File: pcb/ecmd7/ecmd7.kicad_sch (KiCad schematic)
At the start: 75 parts, among them J1 Conn_02x06_Odd_Even, J2 Conn_02x06_Odd_Even, J3 Conn_02x06_Odd_Even, J4 Conn_01x02_Socket, J5 DE9_Socket, J6 Conn_01x04_Socket, Q1 IRFS3806, Q2 IRFS3806, Q3 IRFS3806, Q4 IRFS3806, Q5 IRFS3806, Q6 IRFS3806, Q7 BSC098N10NS5, Q8 BSC098N10NS5, U1 TMC6200-TA, U3 LM5118MH

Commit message: Finalize schematic Add ESD protection Align connector pinout with Arty A7 and Zybo Z7 PMOD
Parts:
- removed J5: DE9_Socket, symbol Connector:DE9_Socket
- removed J6: Conn_01x04_Socket, Connector_PinHeader_1.27mm:PinHeader_1x04_P1.27mm_Vertical, symbol Connector:Conn_01x04_Socket
- removed R44, R45: 4.7k, Resistor_SMD:R_0805_2012Metric, symbol Device:R
- added C11, C38, C42, C43, C57: 100n, Capacitor_SMD:C_0805_2012Metric, symbol Device:C
- added C12, C37, C48: 1u, Capacitor_SMD:C_0805_2012Metric, symbol Device:C
- added D3, D4: SK220ATR, Diode_SMD:D_SMA, symbol Device:D_Schottky
- added D5, D7: MBR0530, Diode_SMD:D_SOD-123, symbol Diode:MBR0530
- added D6, D8: D, Diode_SMD:D_MiniMELF, symbol Device:D
- added J5: Encoder, Connector_PinHeader_2.54mm:PinHeader_2x04_P2.54mm_Vertical, symbol Connector_Generic:Conn_02x04_Odd_Even
- added J7: RS422/BISS-C, Connector_PinHeader_2.54mm:PinHeader_2x03_P2.54mm_Vertical, symbol Connector_Generic:Conn_02x03_Odd_Even
- added JP1, JP3, JP4, JP5, JP7: SolderJumper_2_Open, Jumper:SolderJumper-2_P1.3mm_Open_RoundedPad1.0x1.5mm, symbol Jumper:SolderJumper_2_Open
- added JP2, JP6: SolderJumper_2_Bridged, Jumper:SolderJumper-2_P1.3mm_Bridged_RoundedPad1.0x1.5mm, symbol Jumper:SolderJumper_2_Bridged
- added JP8: SolderJumper_2_Bridged, Jumper:SolderJumper-2_P1.3mm_Open_RoundedPad1.0x1.5mm, symbol Jumper:SolderJumper_2_Bridged
- added L3, L5: 10u, Inductor_SMD:L_TechFuse_SL0530, symbol Device:L
- added L4: 1u, Inductor_SMD:L_0805_2012Metric, symbol Device:L
- added R46, R50: 470, Resistor_SMD:R_0805_2012Metric, symbol Device:R
- added R47: 32k, Resistor_SMD:R_0805_2012Metric, symbol Device:R
- added R48, R51, R64: 10k, Resistor_SMD:R_0805_2012Metric, symbol Device:R
- added R49, R53: 10, Resistor_SMD:R_0805_2012Metric, symbol Device:R
- added R52: 16k, Resistor_SMD:R_0805_2012Metric, symbol Device:R
- added U6: TLV71318PDBV, Package_TO_SOT_SMD:SOT-23-5, symbol Regulator_Linear:TLV71318PDBV
- added U8, U9: LT1616ES6#TRPBF, Package_TO_SOT_SMD:SOT-23-6, symbol ssta_symbols:LT1616ES6#TRPBF
- C29, C30, C31, C32, C33, C34, C35, C36, C40, C55: footprint (none) -> Capacitor_SMD:C_0805_2012Metric
- D1, D2: value D_Schottky -> SK220ATR; footprint (none) -> Diode_SMD:D_SMA
- J1: renamed from J2; value Conn_02x06_Odd_Even -> PMOD_SPI_ENC; footprint Connector_PinHeader_1.27mm:PinHeader_2x06_P1.27mm_Horizontal -> Connector_PinHeader_2.54mm:PinHeader_2x06_P2.54mm_Horizontal
- J2: renamed from J3; value Conn_02x06_Odd_Even -> PMOD_ADC_MPIO; footprint Connector_PinHeader_1.27mm:PinHeader_2x06_P1.27mm_Horizontal -> Connector_PinHeader_2.54mm:PinHeader_2x06_P2.54mm_Horizontal
- J3: renamed from J1; value Conn_02x06_Odd_Even -> PMOD_DRV; footprint Connector_PinHeader_1.27mm:PinHeader_2x06_P1.27mm_Horizontal -> Connector_PinHeader_2.54mm:PinHeader_2x06_P2.54mm_Horizontal
- J4: footprint Connector_AMASS:AMASS_XT60-F_1x02_P7.20mm_Vertical -> Connector_AMASS:AMASS_XT60-M_1x02_P7.20mm_Vertical; symbol Connector:Conn_01x02_Socket -> Connector:Conn_01x02_Pin
- JU1: value Screw_Terminal_01x01 -> Phase U
- JV1: value Screw_Terminal_01x01 -> Phase V
- JW1: value Screw_Terminal_01x01 -> Phase W
- R15: footprint (none) -> Resistor_SMD:R_0805_2012Metric
- U1: footprint eTQFP48_9x9_TRI -> sst_footprints:eTQFP48_9x9_TRI
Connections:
- net +12V: now also D4.1 (K), JP1.2 (B), JP5.2 (B), JP8.2 (B), R46.1, U8.5 (VIN), U9.5 (VIN)
- net +3.3V: now also C48.1, D8.2 (A), JP4.2 (B), JP7.2 (B), L5.2, R52.2; no longer J1.1 (Pin_1), J1.2 (Pin_2), J2.1 (Pin_1), J2.2 (Pin_2), J3.1 (Pin_1), J3.2 (Pin_2)
- net +5V: now also C12.1, D6.2 (A), JP2.2 (B), JP6.2 (B), L3.2, L4.1, R47.2
- net GND: now also C12.2, C37.2, C38.2, C42.2, C48.2, C57.2, D5.2 (A), D7.2 (A), J5.7 (Pin_7), J7.5 (Pin_5), R48.2, R51.2, R64.1, U6.2 (GND), U8.2 (GND), U9.2 (GND)
- net at D1.2 (A), R15.1, U3.12 (CS): now also D3.2 (A)
- net at C33.2, D1.1 (K), L1.1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: now also D3.1 (K)
- net at D2.2 (A), L1.2, Q8.5 (D): now also D4.2 (A)
- net I2C_SCL renamed RS422_TX
- net I2C_SDA renamed RS422_RX
- new net: R47.1, R48.1, U8.3 (FB)
- new net: C43.2, D7.1 (K), L5.1, U9.6 (SW)
- new net: C43.1, D8.1 (K), U9.1 (BOOST)
- new net: C57.1, J7.6 (Pin_6), R53.2
- new net: JP5.1 (A), JP6.1 (A), JP7.1 (A), R53.1
- new net: JP8.1 (A), R50.1
- new net: JP3.2 (B), R50.2, R64.2, U9.4 (~{SHDN})
- new net: C11.1, D6.1 (K), U8.1 (BOOST)
- new net: C11.2, D5.1 (K), L3.1, U8.6 (SW)
- new net: C42.1, J5.8 (Pin_8), R49.2
- new net: R46.2, U8.4 (~{SHDN})
- new net: R51.1, R52.1, U9.3 (FB)
- new net: JP1.1 (A), JP2.1 (A), JP4.1 (A), R49.1
- new net +1V8A: U6.5 (OUT)
- new net +3.3V_IO: J1.1 (Pin_1), J1.2 (Pin_2), J2.1 (Pin_1), J2.2 (Pin_2), J3.1 (Pin_1), J3.2 (Pin_2), JP3.1 (A)
- new net +5VA: C37.1, C38.1, L4.2, U6.1 (IN), U6.3 (EN)
- new net ENC_A_N: J5.1 (Pin_1)
- new net ENC_A_P: J5.2 (Pin_2)
- new net ENC_B_N: J5.3 (Pin_3)
- new net ENC_B_P: J5.4 (Pin_4)
- new net ENC_Z_N: J5.5 (Pin_5)
- new net ENC_Z_P: J5.6 (Pin_6)
- new net RS422_RX_A: J7.4 (Pin_4)
- new net RS422_RX_B: J7.3 (Pin_3)
- new net RS422_TX_A: J7.2 (Pin_2)
- new net RS422_TX_B: J7.1 (Pin_1)
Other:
- sheet Feedback renamed ADC+IO
- sheet ADC+IO: file Feedback.kicad_sch -> ecmd7_adc_io.kicad_sch
- moved on the sheet: C19, C29, C30, C31, C32, C33, C34, C35, C36, C39, C40, C54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

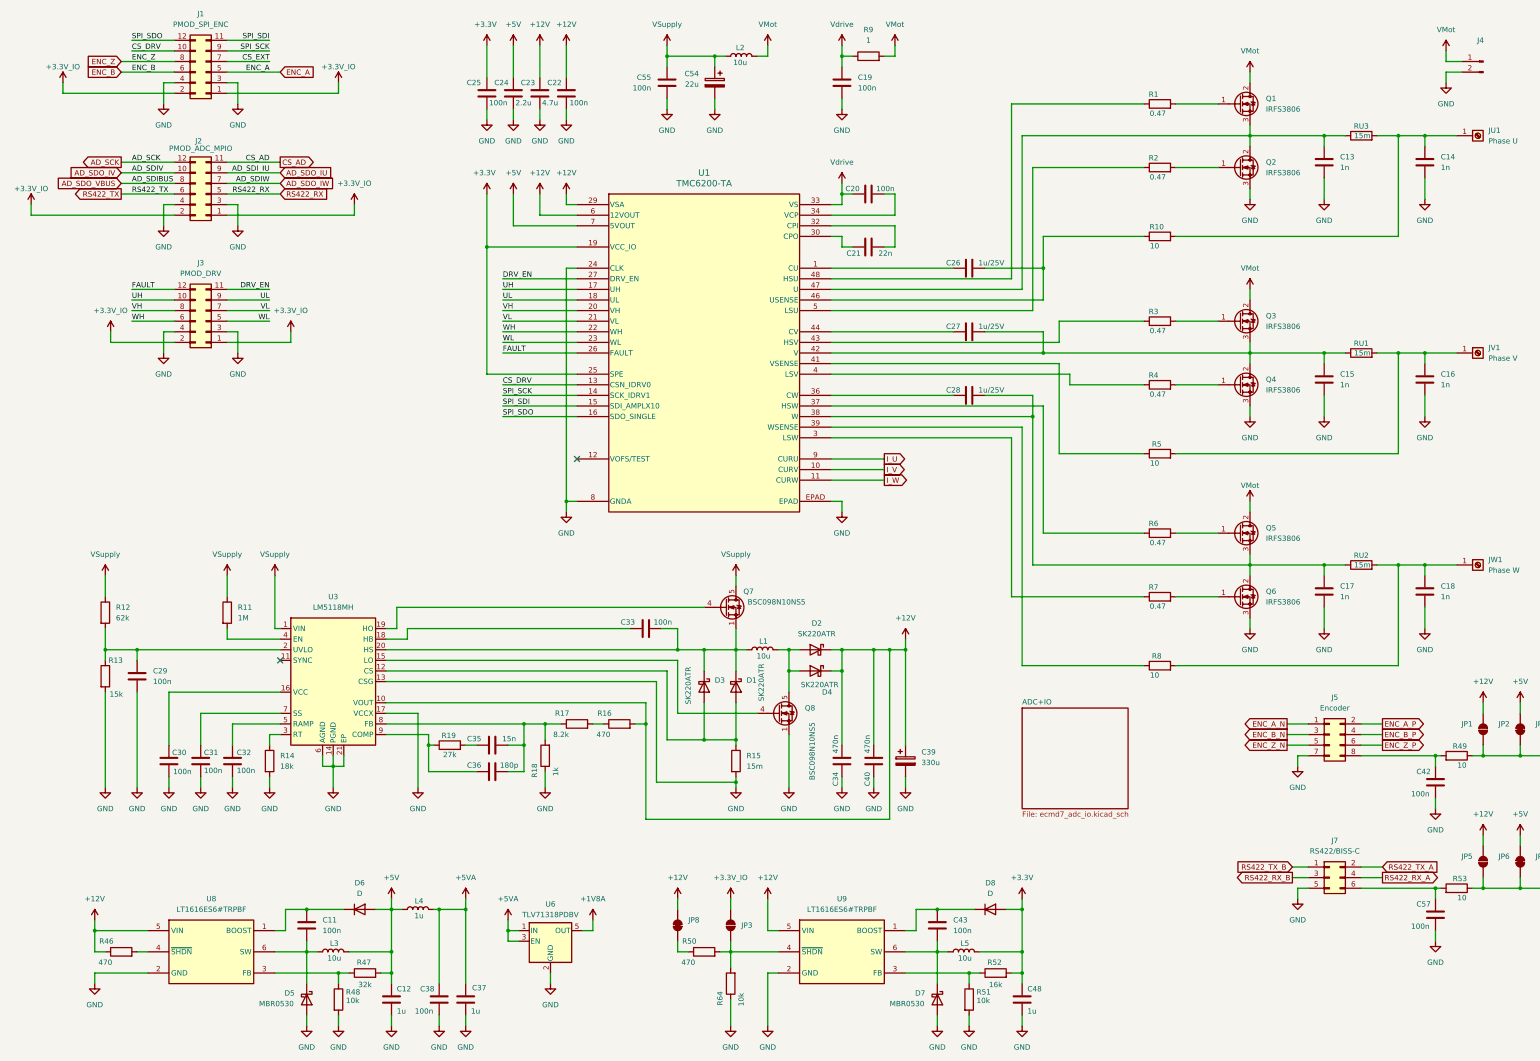
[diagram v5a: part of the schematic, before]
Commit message: Initial component placement
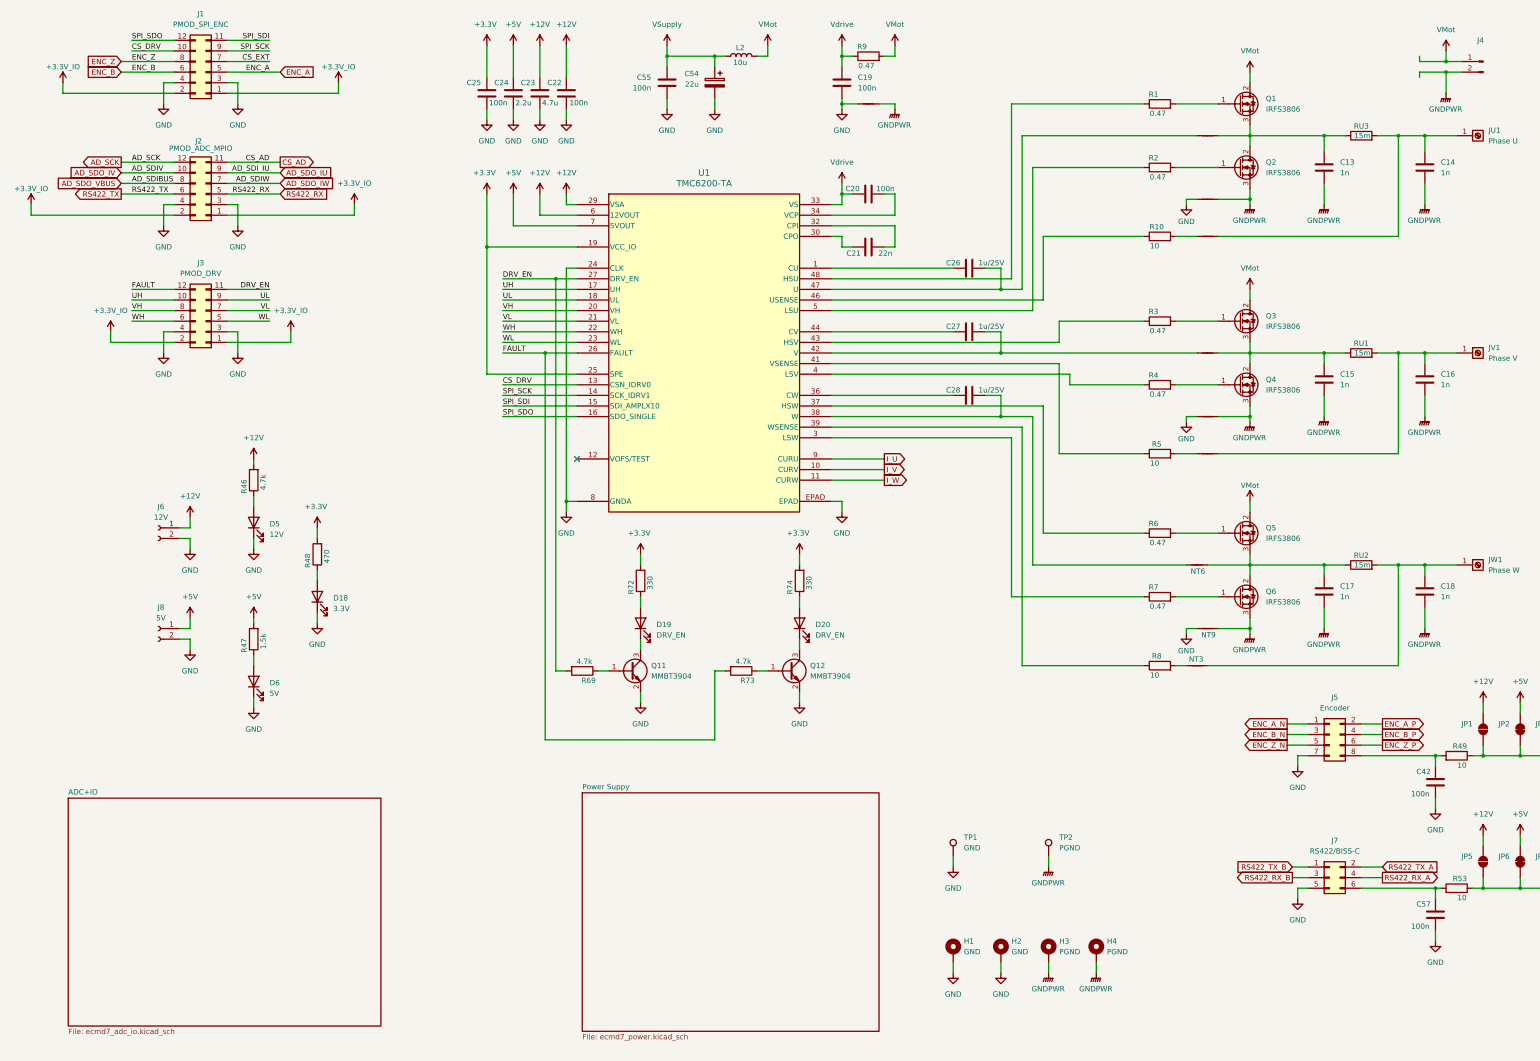
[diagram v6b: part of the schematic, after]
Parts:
- removed C11, C29, C30, C31, C32, C33, C38, C43: 100n, Capacitor_SMD:C_0805_2012Metric, symbol Device:C
- removed C12, C37, C48: 1u, Capacitor_SMD:C_0805_2012Metric, symbol Device:C
- removed C34, C40: 470n, Capacitor_SMD:C_0805_2012Metric, symbol Device:C
- removed C35: 15n, Capacitor_SMD:C_0805_2012Metric, symbol Device:C
- removed C36: 180p, Capacitor_SMD:C_0805_2012Metric, symbol Device:C
- removed C39: 330u, Capacitor_SMD:CP_Elec_6.3x9.9, symbol Device:C_Polarized
- removed D1, D2, D3, D4: SK220ATR, Diode_SMD:D_SMA, symbol Device:D_Schottky
- removed D5, D7: MBR0530, Diode_SMD:D_SOD-123, symbol Diode:MBR0530
- removed D6, D8: D, Diode_SMD:D_MiniMELF, symbol Device:D
- removed JP3: SolderJumper_2_Open, Jumper:SolderJumper-2_P1.3mm_Open_RoundedPad1.0x1.5mm, symbol Jumper:SolderJumper_2_Open
- removed JP8: SolderJumper_2_Bridged, Jumper:SolderJumper-2_P1.3mm_Open_RoundedPad1.0x1.5mm, symbol Jumper:SolderJumper_2_Bridged
- removed L1, L3, L5: 10u, Inductor_SMD:L_TechFuse_SL0530, symbol Device:L
- removed L4: 1u, Inductor_SMD:L_0805_2012Metric, symbol Device:L
- removed Q7, Q8: BSC098N10NS5, Package_TO_SOT_SMD:TDSON-8-1, symbol Transistor_FET:BSC098N10NS5
- removed R11: 1M, Resistor_SMD:R_0805_2012Metric, symbol Device:R
- removed R12: 62k, Resistor_SMD:R_0805_2012Metric, symbol Device:R
- removed R13: 15k, Resistor_SMD:R_0805_2012Metric, symbol Device:R
- removed R14: 18k, Resistor_SMD:R_0805_2012Metric, symbol Device:R
- removed R15: 15m, Resistor_SMD:R_0805_2012Metric, symbol Device:R
- removed R16, R50: 470, Resistor_SMD:R_0805_2012Metric, symbol Device:R
- removed R17: 8.2k, Resistor_SMD:R_0805_2012Metric, symbol Device:R
- removed R18: 1k, Resistor_SMD:R_0805_2012Metric, symbol Device:R
- removed R19: 27k, Resistor_SMD:R_0805_2012Metric, symbol Device:R
- removed R51, R64: 10k, Resistor_SMD:R_0805_2012Metric, symbol Device:R
- removed R52: 16k, Resistor_SMD:R_0805_2012Metric, symbol Device:R
- removed U3: LM5118MH, Package_SO:Texas_PWP0020A, symbol Regulator_Switching:LM5118MH
- removed U6: TLV71318PDBV, Package_TO_SOT_SMD:SOT-23-5, symbol Regulator_Linear:TLV71318PDBV
- removed U8, U9: LT1616ES6#TRPBF, Package_TO_SOT_SMD:SOT-23-6, symbol ssta_symbols:LT1616ES6#TRPBF
- added D18: 3.3V, Diode_SMD:D_0805_2012Metric, symbol Device:LED
- added D19, D20: DRV_EN, Diode_SMD:D_0805_2012Metric, symbol Device:LED
- added D5: 12V, Diode_SMD:D_0805_2012Metric, symbol Device:LED
- added D6: 5V, Diode_SMD:D_0805_2012Metric, symbol Device:LED
- added H1, H2: GND, MountingHole:MountingHole_3.2mm_M3_Pad_Via, symbol Mechanical:MountingHole_Pad
- added H3, H4: PGND, MountingHole:MountingHole_3.2mm_M3_Pad_Via, symbol Mechanical:MountingHole_Pad
- added J6: 12V, Connector_PinHeader_2.00mm:PinHeader_1x02_P2.00mm_Vertical, symbol Connector:Conn_01x02_Socket
- added J8: 5V, Connector_PinHeader_2.00mm:PinHeader_1x02_P2.00mm_Vertical, symbol Connector:Conn_01x02_Socket
- added NT1, NT2, NT3, NT4, NT5, NT6: NetTie_2, NetTie:NetTie-2_SMD_Pad0.5mm, symbol Device:NetTie_2
- added NT10, NT7, NT8, NT9: NetTie_2, NetTie:NetTie-2_SMD_Pad2.0mm, symbol Device:NetTie_2
- added Q11, Q12: MMBT3904, Package_TO_SOT_SMD:SOT-23, symbol Transistor_BJT:MMBT3904
- added R69, R73: 4.7k, Resistor_SMD:R_0805_2012Metric, symbol Device:R
- added R72, R74: 330, Resistor_SMD:R_0805_2012Metric, symbol Device:R
- added TP1: GND, TestPoint:TestPoint_Loop_D2.50mm_Drill1.0mm, symbol Connector:TestPoint
- added TP2: PGND, TestPoint:TestPoint_Loop_D2.50mm_Drill1.0mm, symbol Connector:TestPoint
- JU1, JV1, JW1: footprint MountingHole:MountingHole_3.2mm_M3_Pad_TopBottom -> MountingHole:MountingHole_3.2mm_M3_Pad_Via
- R46: value 470 -> 4.7k
- R47: value 32k -> 1.5k
- R48: value 10k -> 470
- R9: value 1 -> 0.47
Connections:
- net +12V: now also R46.2, J6.1 (Pin_1); no longer R46.1
- net +3.3V: now also R48.2, R72.2, R74.2
- net +5V: now also J8.1 (Pin_1)
- net DRV_EN: now also R69.2
- net FAULT: now also R73.2
- net GND: now also D18.1 (K), D5.1 (K), D6.1 (K), H1.1, H2.1, J6.2 (Pin_2), J8.2 (Pin_2), NT10.2, NT7.2, NT8.2, NT9.2, Q11.2 (E), Q12.2 (E), TP1.1; no longer C13.2, C14.2, C15.2, C16.2, C17.2, C18.2, J4.2 (Pin_2), Q2.3 (S), Q4.3 (S), Q6.3 (S), R48.2
- net at R48.1: now also D18.2 (A); no longer R47.1
- net at C13.1, Q1.3 (S), Q2.2 (D)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: now also NT4.1; no longer U1.47 (U)
- net at C17.1, Q5.3 (S), Q6.2 (D)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: now also NT6.1; no longer C28.1, U1.38 (W)
- net at C18.1, JW1.1 (Pin_1), RU2.2: now also NT3.2; no longer R8.2
- net at R10.1, U1.46 (USENSE): no longer C26.1
- net at C16.1, JV1.1 (Pin_1), RU1.2: now also NT2.2; no longer R5.2
- net at C14.1, JU1.1 (Pin_1), RU3.2: now also NT1.1; no longer R10.2
- net at C15.1, Q3.3 (S), Q4.2 (D)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: now also NT5.1; no longer C27.1, U1.42 (V)
- new net: NT1.2, R10.2
- new net: C26.1, NT4.2, U1.47 (U)
- new net: NT2.1, R5.2
- new net: NT3.1, R8.2
- new net: Q12.1 (B), R73.1
- new net: D20.1 (K), Q12.3 (C)
- new net: Q11.1 (B), R69.1
- new net: D6.2 (A), R47.1
- new net: D19.1 (K), Q11.3 (C)
- new net: D19.2 (A), R72.1
- new net: C28.1, NT6.2, U1.38 (W)
- new net: C27.1, NT5.2, U1.42 (V)
- new net: D5.2 (A), R46.1
- new net: D20.2 (A), R74.1
- new net GNDPWR: C13.2, C14.2, C15.2, C16.2, C17.2, C18.2, H3.1, H4.1, J4.2 (Pin_2), NT10.1, NT7.1, NT8.1, NT9.1, Q2.3 (S), Q4.3 (S), Q6.3 (S), TP2.1
- no-connect marks 2 -> 1
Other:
- added sheet Power Suppy (ecmd7_power.kicad_sch)
- moved on the sheet: C13, C14
